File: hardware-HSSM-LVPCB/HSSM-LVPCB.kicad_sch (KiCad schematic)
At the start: 57 parts, among them J1 UFL_R_SMT_1_10, J2 LPPB061NGCN-RC, Q1 Q_MOSFET_N_BSS123, Q2 Q_MOSFET_N_BSS123, U1 ESP32-C6, U2 W25Q64JVSSIQ_SOIC-8, X1 X_40MHz_SMD_ECS-2520SMV-400-F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

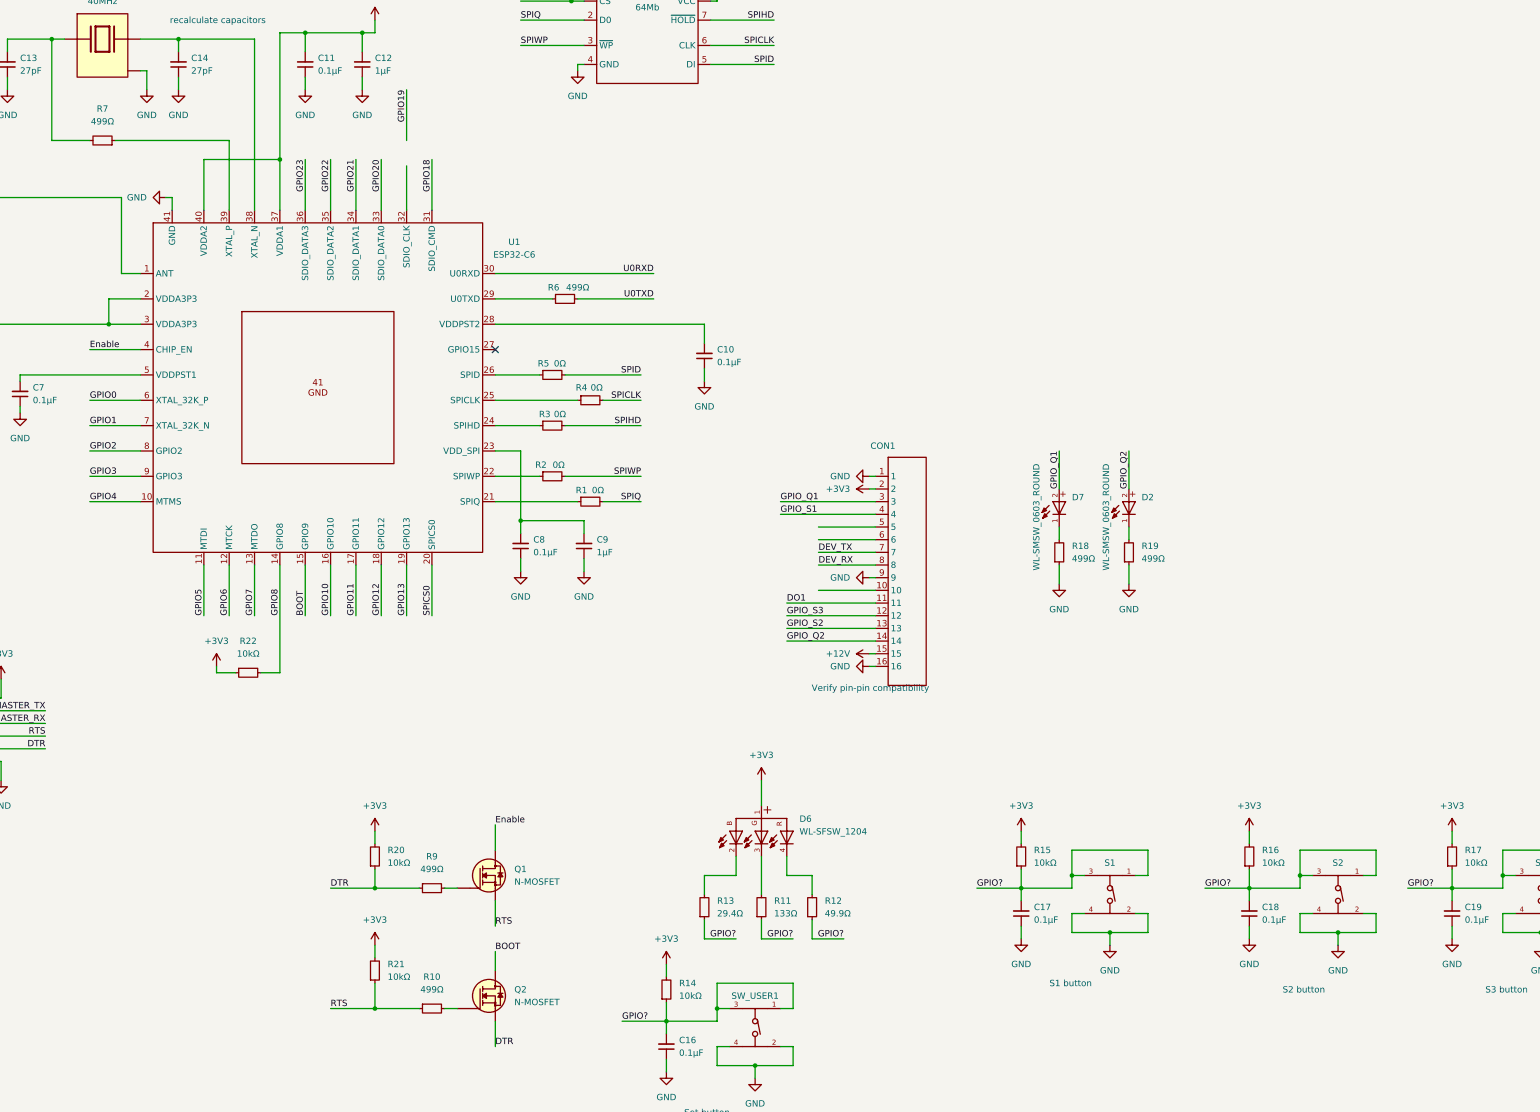
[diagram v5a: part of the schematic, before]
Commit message: [#4] SCH connect GPIOs
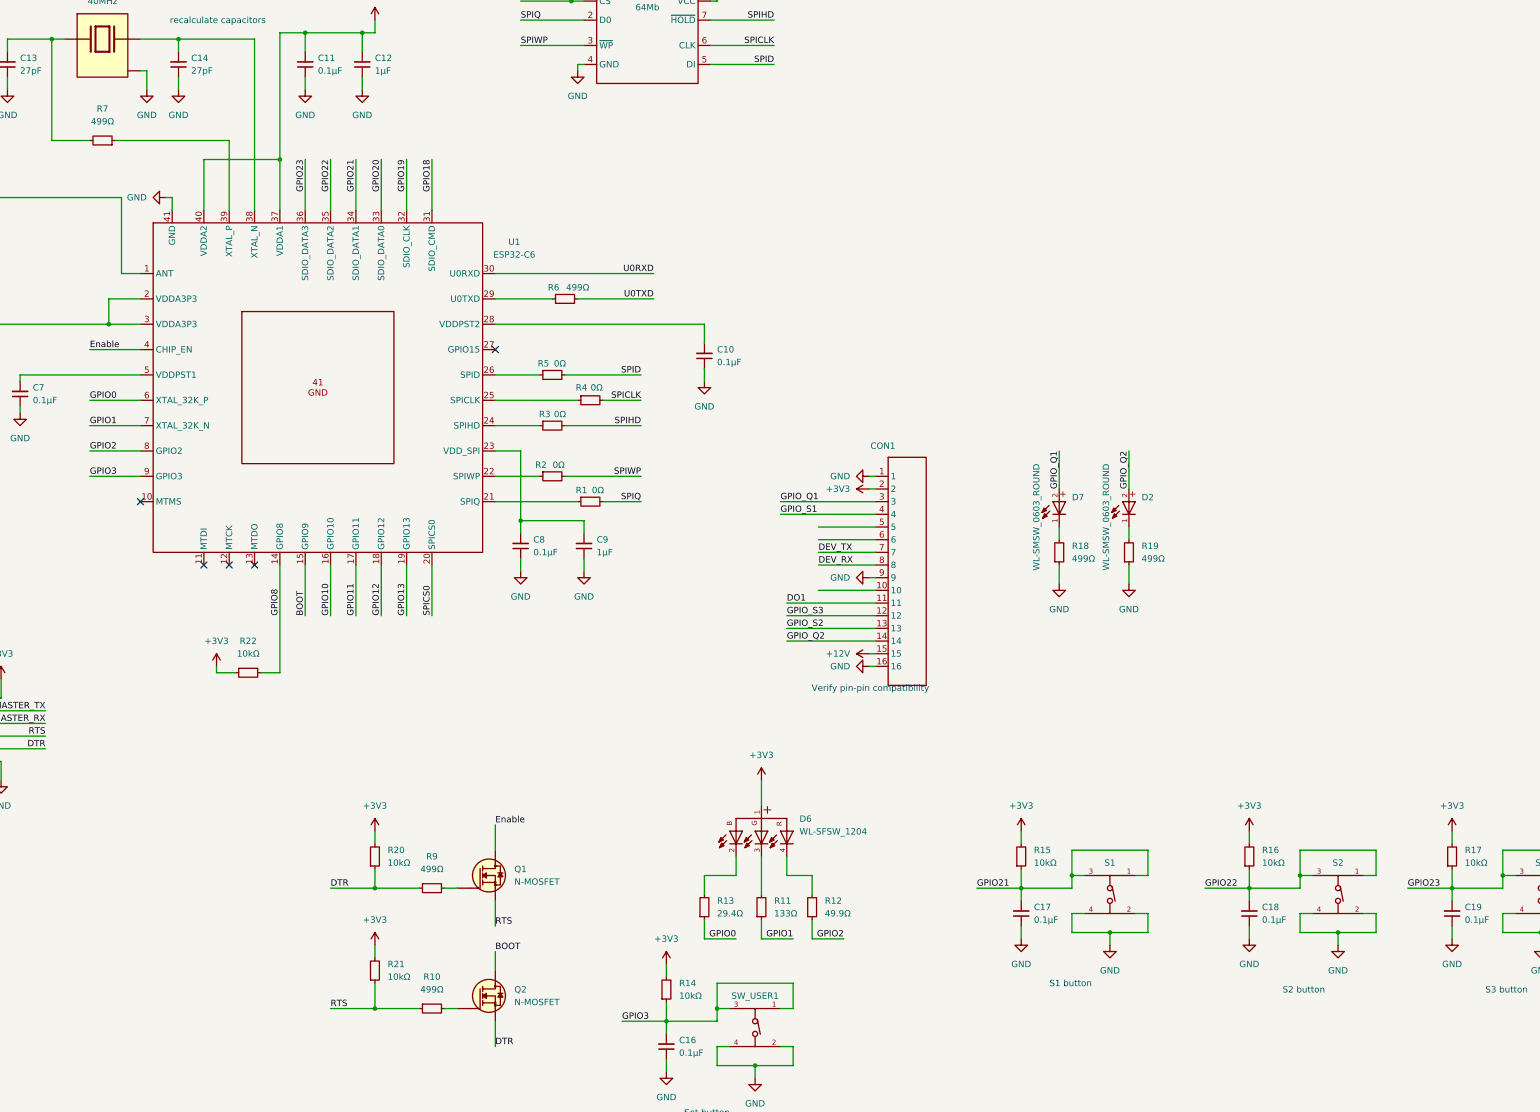
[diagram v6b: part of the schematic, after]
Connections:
- net GPIO0: now also R13.1
- net GPIO1: now also R11.1
- net GPIO19: now also U1.32 (SDIO_CLK)
- net GPIO2: now also R12.1
- net GPIO21: now also C17.2, R15.1, S1.1, S1.3
- net GPIO22: now also C18.2, R16.1, S2.1, S2.3
- net GPIO23: now also C19.2, R17.1, S3.1, S3.3
- net GPIO3: now also C16.2, R14.1, SW_USER1.1, SW_USER1.3
- net GPIO4: no longer names the net of U1.10 (MTMS)
- net GPIO5: no longer names the net of U1.11 (MTDI)
- net GPIO6: no longer names the net of U1.12 (MTCK)
- net GPIO7: no longer names the net of U1.13 (MTDO)
- removed net GPIO?: C16.2, C17.2, C18.2, C19.2, R11.1, R12.1, R13.1, R14.1, R15.1, R16.1, R17.1, S1.1, S1.3, S2.1, S2.3, S3.1, S3.3, SW_USER1.1, SW_USER1.3
- no-connect marks 1 -> 5
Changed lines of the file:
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@@
+	)
+	(no_connect
+		(at 116.84 154.94)
 	)
 	(no_connect
 		(at 175.26 111.76)
 	)
+	(no_connect
+		(at 127 154.94)
+	)
+	(no_connect
+		(at 104.14 142.24)
+	)
+	(no_connect
+		(at 121.92 154.94)
+	)
 	(wire
 		(pts
@@
 	(wire
 		(pts
-			(xy 157.48 74.93) (xy 157.48 83.82)
-		)
-		(stroke
-			(width 0)
-			(type default)
-		)
-	)
-	(wire
-		(pts
 			(xy 175.26 106.68) (xy 217.17 106.68)
 		)
@@
 	(wire
 		(pts
-			(xy 127 165.1) (xy 127 154.94)
-		)
-		(stroke
-			(width 0)
-			(type default)
-		)
-	)
-	(wire
-		(pts
 			(xy 137.16 48.26) (xy 137.16 52.07)
 		)
@@
 	(wire
 		(pts
-			(xy 93.98 142.24) (xy 104.14 142.24)
-		)
-		(stroke
-			(width 0)
-			(type default)
-		)
-	)
-	(wire
-		(pts
 			(xy 180.34 50.8) (xy 193.04 50.8)
 		)
@@
 	(wire
 		(pts
-			(xy 116.84 165.1) (xy 116.84 154.94)
-		)
-		(stroke
-			(width 0)
-			(type default)
-		)
-	)
-	(wire
-		(pts
 			(xy 306.07 217.17) (xy 306.07 212.09)
 		)
@@
 	(wire
 		(pts
-			(xy 121.92 165.1) (xy 121.92 154.94)
-		)
-		(stroke
-			(width 0)
-			(type default)
-		)
-	)
-	(wire
-		(pts
 			(xy 218.44 41.91) (xy 219.71 41.91)
 		)
@@
 	(wire
 		(pts
-			(xy 157.48 59.69) (xy 157.48 69.85)
+			(xy 157.48 73.66) (xy 157.48 83.82)
 		)
 		(stroke
@@
 		)
 	)
-	(label "GPIO?"
+	(label "GPIO2"
 		(at 245.11 229.87 180)
 		(fields_autoplaced yes)
@@
 		)
 	)
-	(label "GPIO?"
+	(label "GPIO22"
 		(at 317.5 219.71 0)
 		(fields_autoplaced yes)
@@
 		)
 	)
-	(label "GPIO4"
-		(at 93.98 142.24 0)
-		(fields_autoplaced yes)
-		(effects
-			(font
-				(size 1.27 1.27)
-			)
-			(justify left bottom)
-		)
-	)
 	(label "Enable"
 		(at 93.98 111.76 0)
@@
 		)
 	)
-	(label "GPIO7"
-		(at 127 165.1 90)
-		(fields_autoplaced yes)
-		(effects
-			(font
-				(size 1.27 1.27)
-			)
-			(justify left bottom)
-		)
-	)
 	(label "DTR"
 		(at 142.24 219.71 0)
@@
 	)
 	(label "GPIO19"
-		(at 157.48 59.69 270)
+		(at 157.48 73.66 270)
 		(fields_autoplaced yes)
 		(effects
@@
 		)
 	)
-	(label "GPIO?"
+	(label "GPIO0"
 		(at 223.52 229.87 180)
 		(fields_autoplaced yes)
@@
 		)
 	)
-	(label "GPIO?"
+	(label "GPIO21"
 		(at 271.78 219.71 0)
 		(fields_autoplaced yes)
@@
 		)
 	)
-	(label "GPIO?"
+	(label "GPIO1"
 		(at 234.95 229.87 180)
 		(fields_autoplaced yes)
@@
 		)
 	)
-	(label "GPIO?"
+	(label "GPIO23"
 		(at 358.14 219.71 0)
 		(fields_autoplaced yes)
@@
 		)
 	)
-	(label "GPIO5"
-		(at 116.84 165.1 90)
-		(fields_autoplaced yes)
-		(effects
-			(font
-				(size 1.27 1.27)
-			)
-			(justify left bottom)
-		)
-	)
-	(label "GPIO?"
+	(label "GPIO3"
 		(at 200.66 246.38 0)
 		(fields_autoplaced yes)
@@
 		(fields_autoplaced yes)
 		(effects
-			(font
-				(size 1.27 1.27)
-			)
-			(justify left bottom)
-		)
-	)
-	(label "GPIO6"
-		(at 121.92 165.1 90)
-		(fields_autoplaced yes)
-		(effects

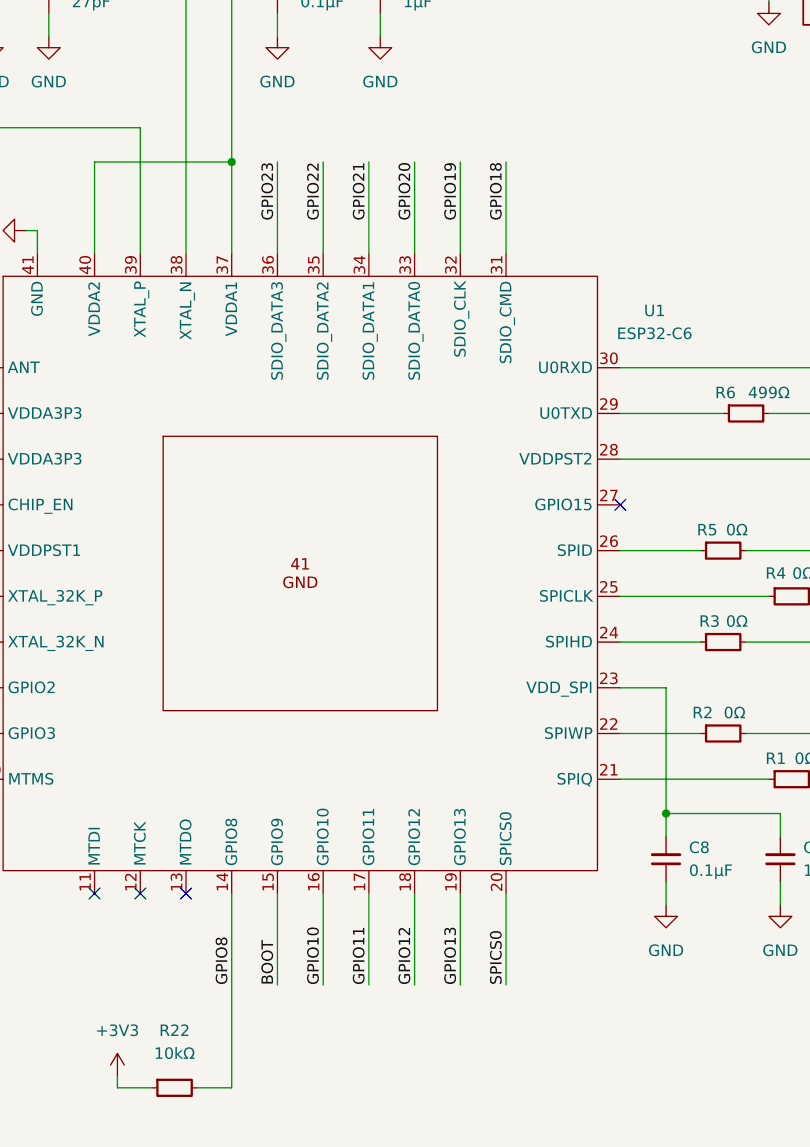
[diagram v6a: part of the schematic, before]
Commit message: [#4] SCH connect GPIOs
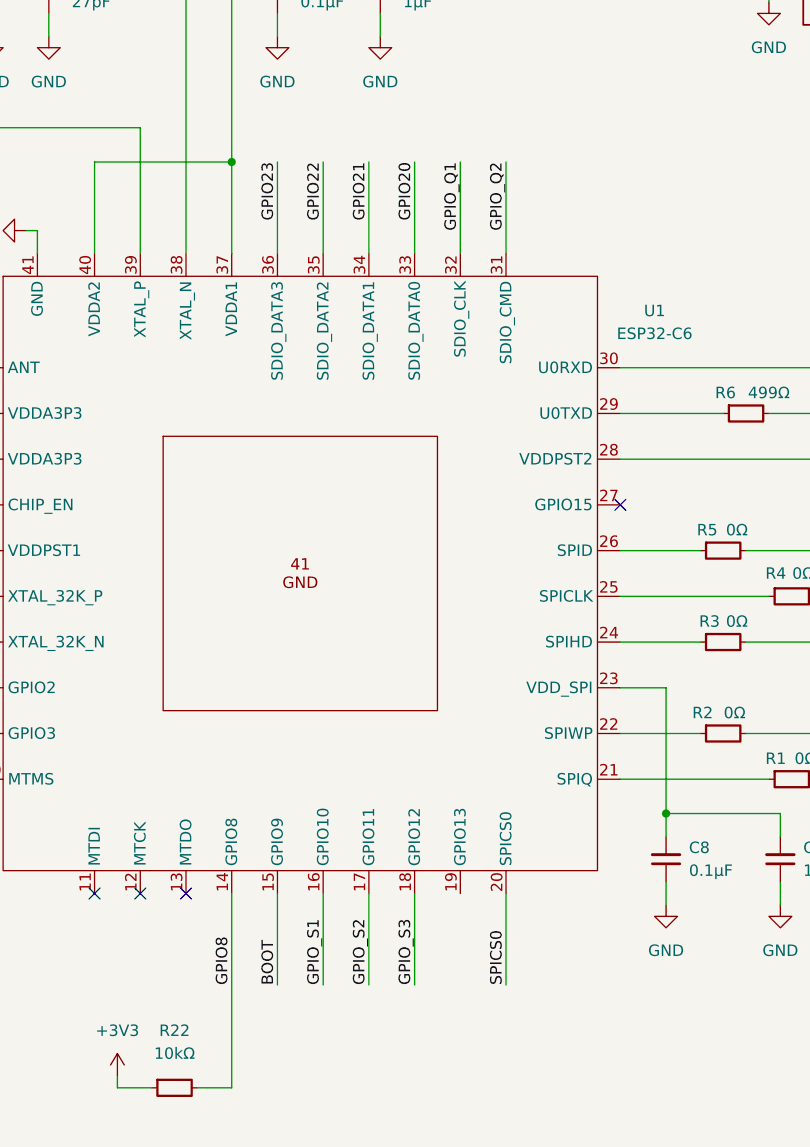
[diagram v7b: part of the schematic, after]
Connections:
- net GPIO10 is gone; now on net GPIO_S1: U1.16 (GPIO10)
- net GPIO11 is gone; now on net GPIO_S2: U1.17 (GPIO11)
- net GPIO12 is gone; now on net GPIO_S3: U1.18 (GPIO12)
- net GPIO18 is gone; now on net GPIO_Q2: U1.31 (SDIO_CMD)
- net GPIO19 is gone; now on net GPIO_Q1: U1.32 (SDIO_CLK)
- net GPIO13: no longer names the net of U1.19 (GPIO13)

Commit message: [#9] PCB placement WIP
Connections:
- net GPIO3: now also U1.19 (GPIO13); no longer U1.9 (GPIO3)
- no-connect marks 5 -> 6
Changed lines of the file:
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@@
+	)
+	(no_connect
+		(at 104.14 137.16)
 	)
 	(no_connect
@@
 	(wire
 		(pts
+			(xy 157.48 165.1) (xy 157.48 154.94)
+		)
+		(stroke
+			(width 0)
+			(type default)
+		)
+	)
+	(wire
+		(pts
 			(xy 326.39 215.9) (xy 326.39 219.71)
 		)
@@
 		(pts
 			(xy 80.01 123.19) (xy 80.01 124.46)
-		)
-		(stroke
-			(width 0)
-			(type default)
-		)
-	)
-	(wire
-		(pts
-			(xy 93.98 137.16) (xy 104.14 137.16)
 		)
 		(stroke
@@
 		)
 	)
-	(label "GPIO3"
-		(at 93.98 137.16 0)
-		(fields_autoplaced yes)
-		(effects
-			(font
-				(size 1.27 1.27)
-			)
-			(justify left bottom)
-		)
-	)
 	(label "GPIO_Q2"
 		(at 162.56 73.66 270)
@@
 		(fields_autoplaced yes)
 		(effects
+			(font
+				(size 1.27 1.27)
+			)
+			(justify left bottom)
+		)
+	)
+	(label "GPIO3"
+		(at 157.48 165.1 90)
+		(fields_autoplaced yes)
+		(effects
